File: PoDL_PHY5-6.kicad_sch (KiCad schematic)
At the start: 45 parts, among them Q32 DMG3414U, Q33 MMBTA06, Q34 MMBT3904, Q35 DMG3414U, Q36 DMG3414U, Q37 MMBT3904, Q38 DMG3414U, Q39 MMBTA06, Q40 MMBT3904, Q41 DMG3414U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

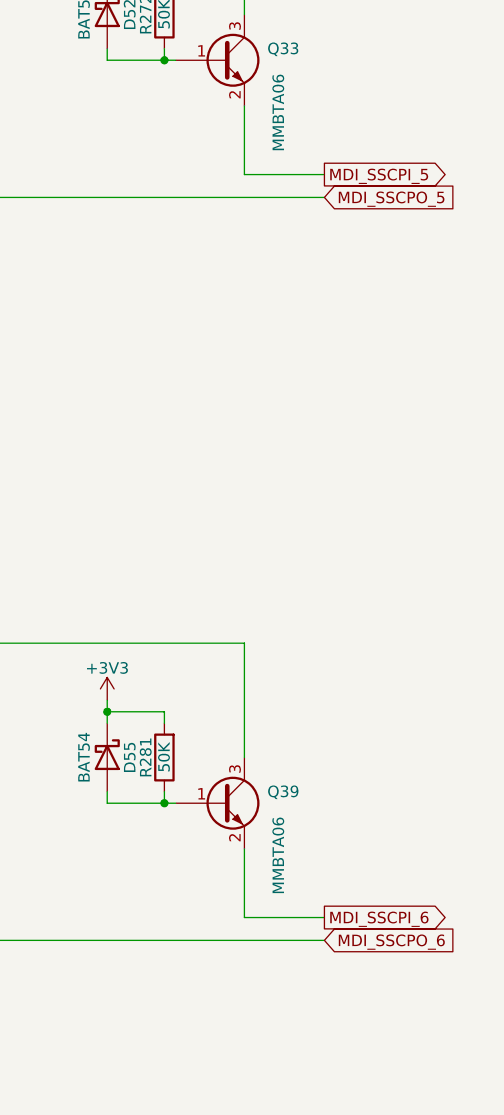
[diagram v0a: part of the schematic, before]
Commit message: Correcting SCCP spelling
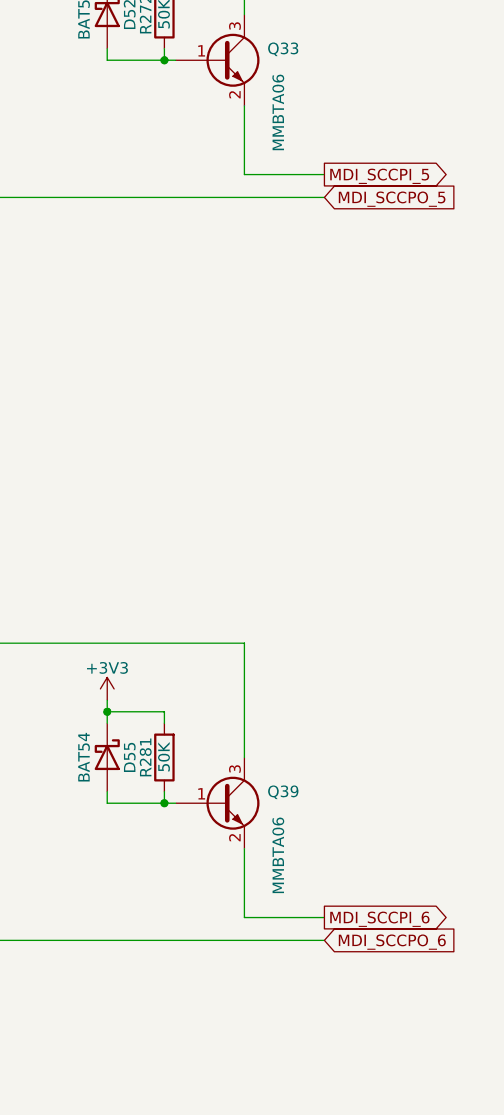
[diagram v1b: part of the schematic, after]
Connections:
- net MDI_SSCPI_5 renamed MDI_SCCPI_5
- net MDI_SSCPI_6 renamed MDI_SCCPI_6
- net MDI_SSCPO_5 renamed MDI_SCCPO_5
- net MDI_SSCPO_6 renamed MDI_SCCPO_6
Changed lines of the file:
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@@
     )
   )
-  (global_label "MDI_SSCPO_6" (shape input) (at 198.12 143.51 0) (fields_autoplaced)
+  (global_label "MDI_SCCPO_6" (shape input) (at 198.12 143.51 0) (fields_autoplaced)
     (effects (font (size 1.27 1.27)) (justify left))
     (property "Intersheet References" "${INTERSHEET_REFS}" (id 0) (at 213.2936 143.4306 0)
@@
     )
   )
-  (global_label "MDI_SSCPO_5" (shape input) (at 198.12 60.96 0) (fields_autoplaced)
+  (global_label "MDI_SCCPO_5" (shape input) (at 198.12 60.96 0) (fields_autoplaced)
     (effects (font (size 1.27 1.27)) (justify left))
     (property "Intersheet References" "${INTERSHEET_REFS}" (id 0) (at 213.2936 60.8806 0)
@@
     )
   )
-  (global_label "MDI_SSCPI_5" (shape output) (at 198.12 58.42 0) (fields_autoplaced)
+  (global_label "MDI_SCCPI_5" (shape output) (at 198.12 58.42 0) (fields_autoplaced)
     (effects (font (size 1.27 1.27)) (justify left))
     (property "Intersheet References" "${INTERSHEET_REFS}" (id 0) (at 212.5679 58.3406 0)
@@
     )
   )
-  (global_label "MDI_SSCPI_6" (shape output) (at 198.12 140.97 0) (fields_autoplaced)
+  (global_label "MDI_SCCPI_6" (shape output) (at 198.12 140.97 0) (fields_autoplaced)
     (effects (font (size 1.27 1.27)) (justify left))
     (property "Intersheet References" "${INTERSHEET_REFS}" (id 0) (at 212.5679 140.8906 0)
